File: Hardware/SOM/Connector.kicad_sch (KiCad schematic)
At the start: 1 part, among them J1 SODIMM-200_Split

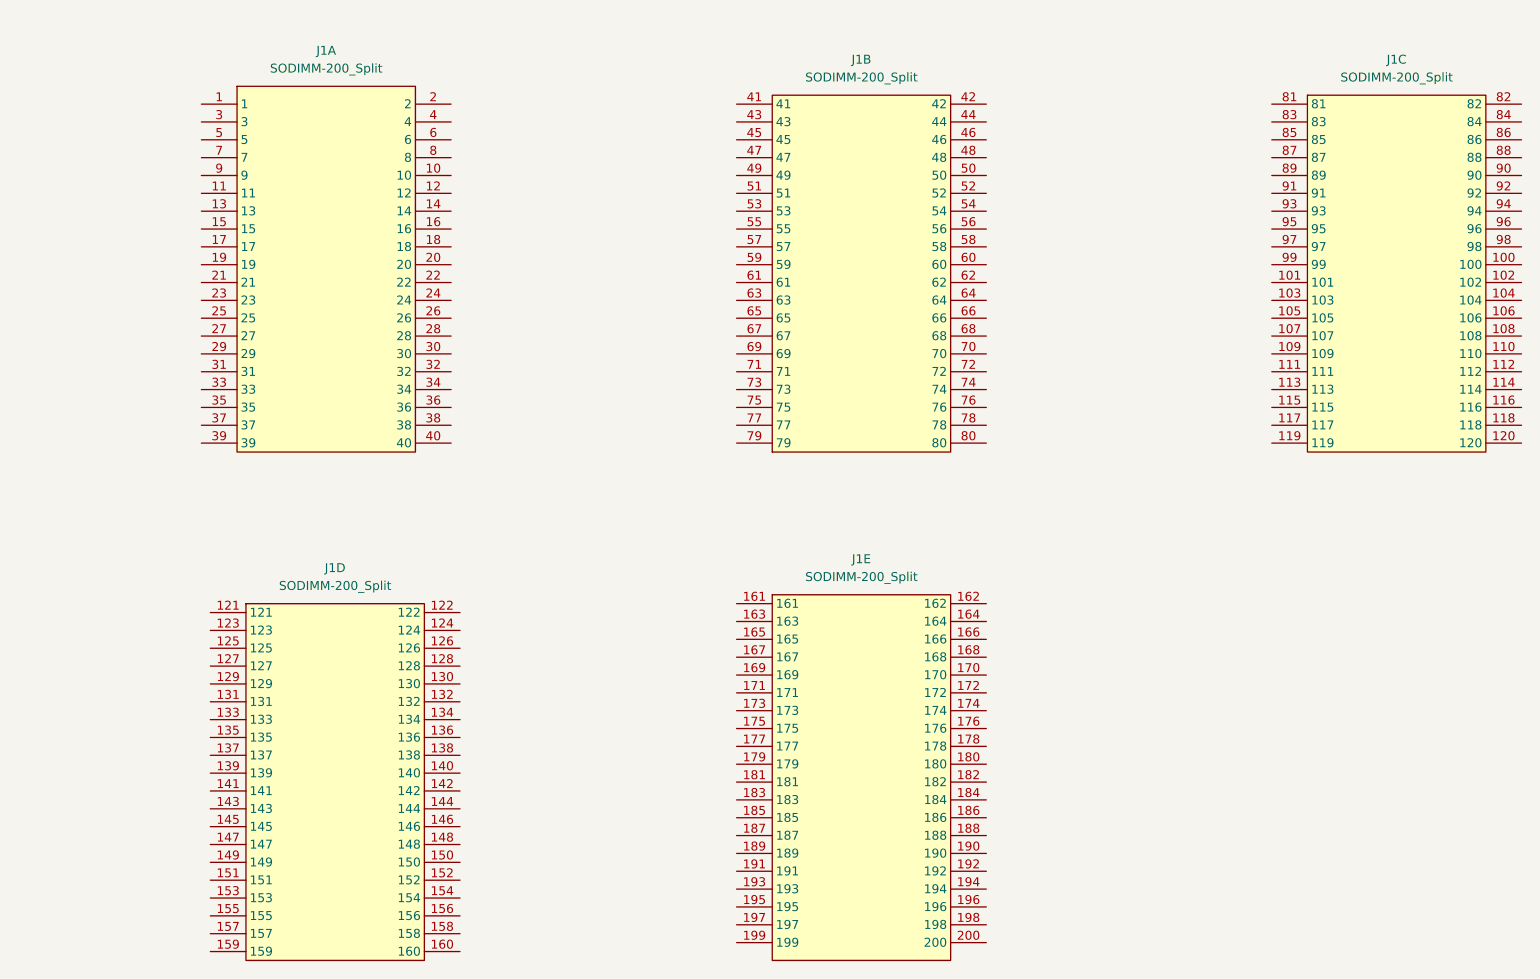
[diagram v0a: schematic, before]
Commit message: BB SOM connector
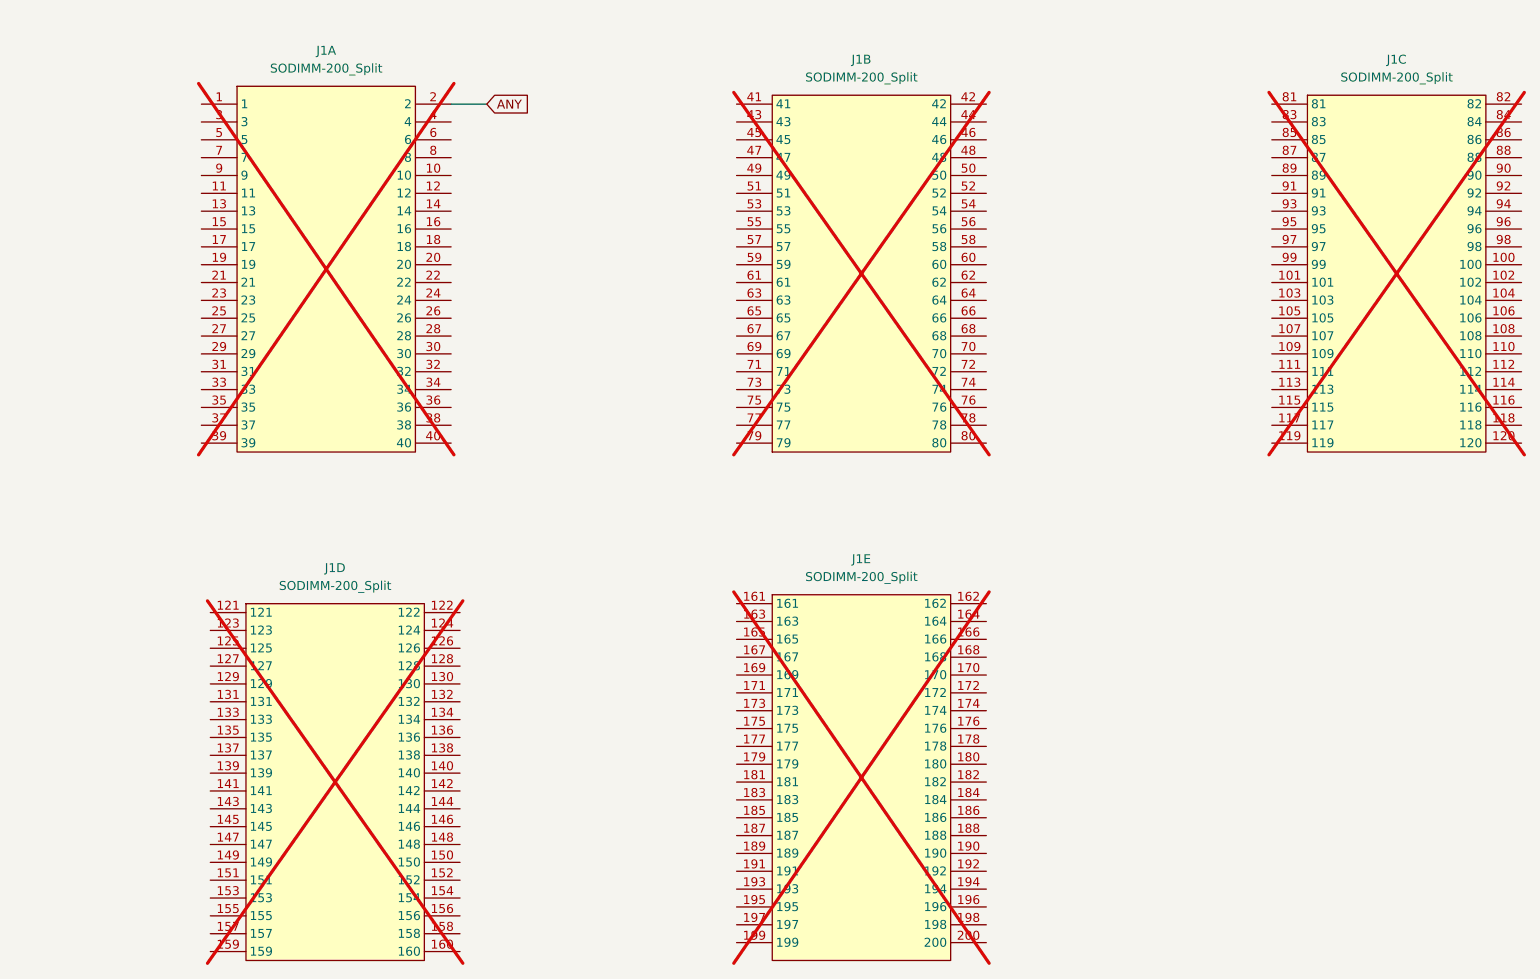
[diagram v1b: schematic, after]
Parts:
- J1: now not fitted
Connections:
- net ANY: now reaches J1.2
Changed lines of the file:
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@@
 	(generator_version "9.0")
 	(paper "A4")
+	(wire
+		(pts
+			(xy 81.28 30.48) (xy 86.36 30.48)
+		)
+		(stroke
+			(width 0)
+			(type default)
+		)
+	)
+	(global_label "ANY"
+		(shape input)
+		(at 86.36 30.48 0)
+		(fields_autoplaced yes)
+		(effects
+			(font
+				(size 1.27 1.27)
+			)
+			(justify left)
+		)
+		(property "Intersheetrefs" "${INTERSHEET_REFS}"
+			(at 92.8529 30.48 0)
+			(effects
+				(font
+					(size 1.27 1.27)
+				)
+				(justify left)
+				(hide yes)
+			)
+		)
+	)
 	(symbol
 		(lib_id "Connector:SODIMM-200_Split")
@@
 		(in_bom yes)
 		(on_board yes)
-		(dnp no)
+		(dnp yes)
 		(fields_autoplaced yes)
 		(property "Reference" "J1"
@@
 		(in_bom yes)
 		(on_board yes)
-		(dnp no)
+		(dnp yes)
 		(fields_autoplaced yes)
 		(property "Reference" "J1"
@@
 		(in_bom yes)
 		(on_board yes)
-		(dnp no)
+		(dnp yes)
 		(fields_autoplaced yes)
 		(property "Reference" "J1"
@@
 		(in_bom yes)
 		(on_board yes)
-		(dnp no)
+		(dnp yes)
 		(fields_autoplaced yes)
 		(property "Reference" "J1"
@@
 		(in_bom yes)
 		(on_board yes)
-		(dnp no)
+		(dnp yes)
 		(fields_autoplaced yes)
 		(property "Reference" "J1"

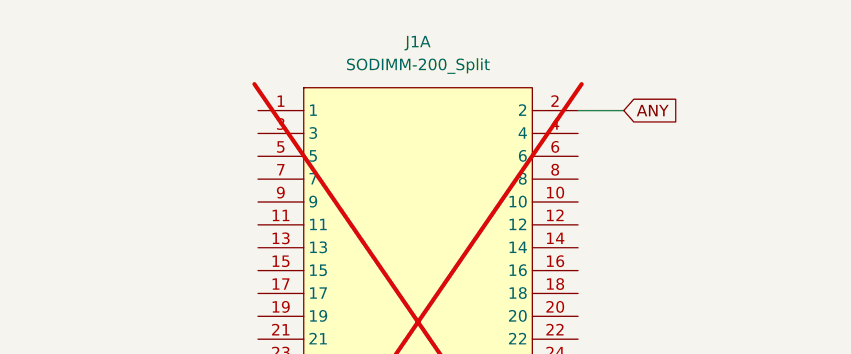
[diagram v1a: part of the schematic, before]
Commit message: QSPI, banks IO decoupling
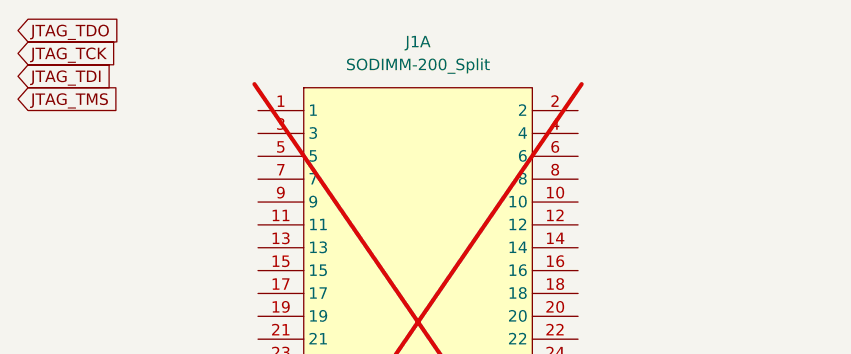
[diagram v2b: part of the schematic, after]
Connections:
- net ANY: no longer names the net of J1.2
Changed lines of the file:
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@@
 	(generator_version "9.0")
 	(paper "A4")
-	(wire
-		(pts
-			(xy 81.28 30.48) (xy 86.36 30.48)
-		)
-		(stroke
-			(width 0)
-			(type default)
-		)
-	)
-	(global_label "ANY"
+	(global_label "JTAG_TDI"
 		(shape input)
-		(at 86.36 30.48 0)
+		(at 19.05 26.67 0)
 		(fields_autoplaced yes)
 		(effects
@@
 		)
 		(property "Intersheetrefs" "${INTERSHEET_REFS}"
-			(at 92.8529 30.48 0)
+			(at 30.139 26.67 0)
 			(effects
 				(font
+					(size 1.27 1.27)
+				)
+				(justify left)
+				(hide yes)
+			)
+		)
+	)
+	(global_label "JTAG_TCK"
+		(shape input)
+		(at 19.05 24.13 0)
+		(fields_autoplaced yes)
+		(effects
+			(font
+				(size 1.27 1.27)
+			)
+			(justify left)
+		)
+		(property "Intersheetrefs" "${INTERSHEET_REFS}"
+			(at 30.8042 24.13 0)
+			(effects
+				(font
+					(size 1.27 1.27)
+				)
+				(justify left)
+				(hide yes)
+			)
+		)
+	)
+	(global_label "JTAG_TDO"
+		(shape input)
+		(at 19.05 21.59 0)
+		(fields_autoplaced yes)
+		(effects
+			(font
+				(size 1.27 1.27)
+			)
+			(justify left)
+		)
+		(property "Intersheetrefs" "${INTERSHEET_REFS}"
+			(at 30.8647 21.59 0)
+			(effects
+				(font
+					(size 1.27 1.27)
+				)
+				(justify left)
+				(hide yes)
+			)
+		)
+	)
+	(global_label "JTAG_TMS"
+		(shape input)
+		(at 19.05 29.21 0)
+		(fields_autoplaced yes)
+		(effects
+			(font
+				(size 1.27 1.27)
+			)
+			(justify left)
+		)
+		(property "Intersheetrefs" "${INTERSHEET_REFS}"
+			(at 30.9251 29.21 0)
+			(effects
+				(font

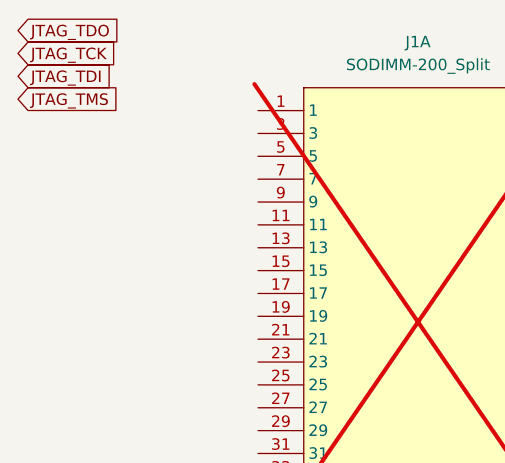
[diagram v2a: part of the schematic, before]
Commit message: SOM: Boot mode CFG
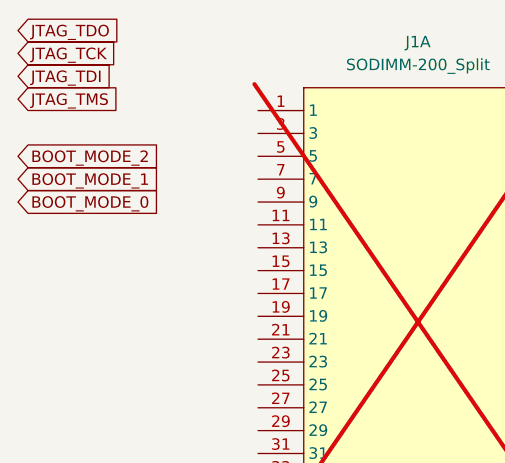
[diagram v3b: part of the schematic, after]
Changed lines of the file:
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@@
+		)
+	)
+	(global_label "BOOT_MODE_2"
+		(shape input)
+		(at 19.05 35.56 0)
+		(fields_autoplaced yes)
+		(effects
+			(font
+				(size 1.27 1.27)
+			)
+			(justify left)
+		)
+		(property "Intersheetrefs" "${INTERSHEET_REFS}"
+			(at 35.2794 35.56 0)
+			(effects
+				(font
+					(size 1.27 1.27)
+				)
+				(justify left)
+				(hide yes)
+			)
 		)
 	)
@@
 		)
 	)
+	(global_label "BOOT_MODE_1"
+		(shape input)
+		(at 19.05 38.1 0)
+		(fields_autoplaced yes)
+		(effects
+			(font
+				(size 1.27 1.27)
+			)
+			(justify left)
+		)
+		(property "Intersheetrefs" "${INTERSHEET_REFS}"
+			(at 35.2794 38.1 0)
+			(effects
+				(font
+					(size 1.27 1.27)
+				)
+				(justify left)
+				(hide yes)
+			)
+		)
+	)
 	(global_label "JTAG_TDO"
 		(shape input)
@@
 			(effects
 				(font
+					(size 1.27 1.27)
+				)
+				(justify left)
+				(hide yes)
+			)
+		)
+	)
+	(global_label "BOOT_MODE_0"
+		(shape input)
+		(at 19.05 40.64 0)
+		(fields_autoplaced yes)
+		(effects
+			(font
+				(size 1.27 1.27)
+			)
+			(justify left)
+		)
+		(property "Intersheetrefs" "${INTERSHEET_REFS}"
+			(at 35.2794 40.64 0)
+			(effects
+				(font

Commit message: DDR Banks Vref
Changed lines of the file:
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@@
+		)
+	)
+	(global_label "DONE"
+		(shape input)
+		(at 19.05 19.05 0)
+		(fields_autoplaced yes)
+		(effects
+			(font
+				(size 1.27 1.27)
+			)
+			(justify left)
+		)
+		(property "Intersheetrefs" "${INTERSHEET_REFS}"
+			(at 27.1152 19.05 0)
+			(effects
+				(font
+					(size 1.27 1.27)
+				)
+				(justify left)
+				(hide yes)
+			)
 		)
 	)

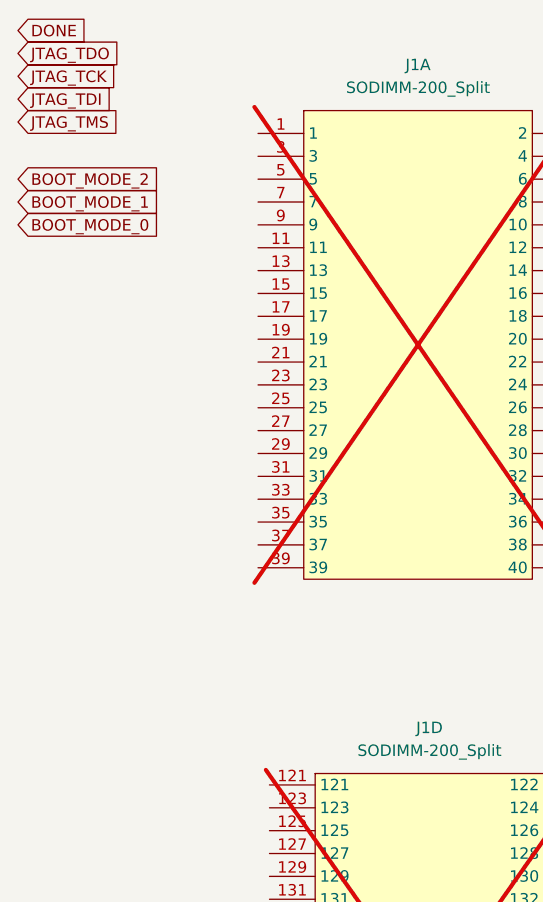
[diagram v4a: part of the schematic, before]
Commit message: SOM: power supply update
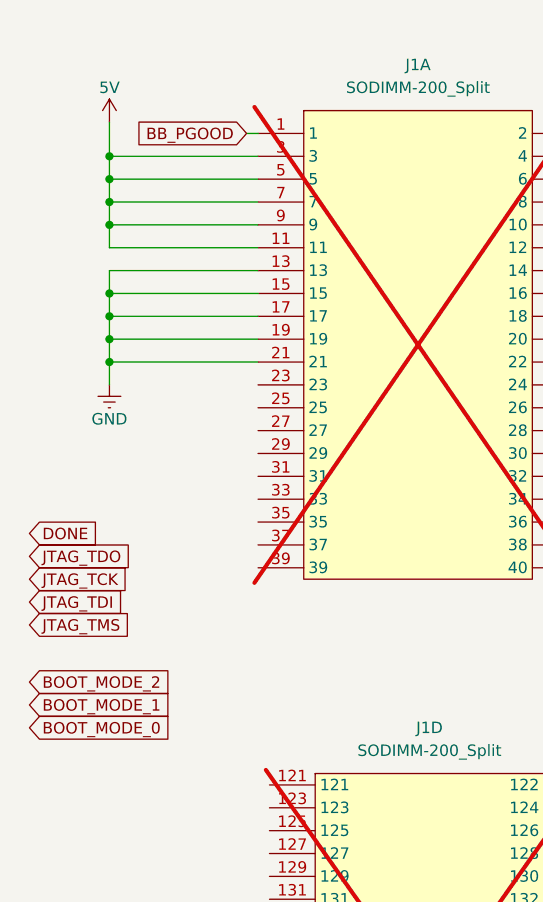
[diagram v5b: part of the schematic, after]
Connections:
- net BB_PGOOD: now reaches J1.1
- net 5V: now reaches J1.11
- net 5V: now also J1.3, J1.5, J1.7, J1.9
- net GND: now reaches J1.13
- net GND: now also J1.15, J1.17, J1.19, J1.21

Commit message: SOM: layout update
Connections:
- net 5V: now also J1.10, J1.2, J1.4, J1.6, J1.8
- net GND: now also J1.14, J1.16, J1.18, J1.20, J1.22
- no-connect marks 0 -> 1
